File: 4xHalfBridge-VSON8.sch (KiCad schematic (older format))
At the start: 76 parts, among them U1 VSON8_Nexfet, U2 VSON8_Nexfet, U3 VSON8_Nexfet, U4 VSON8_Nexfet, U5 VSON8_Nexfet, U6 VSON8_Nexfet, U7 VSON8_Nexfet, U8 VSON8_Nexfet, U9 PowerStage_L

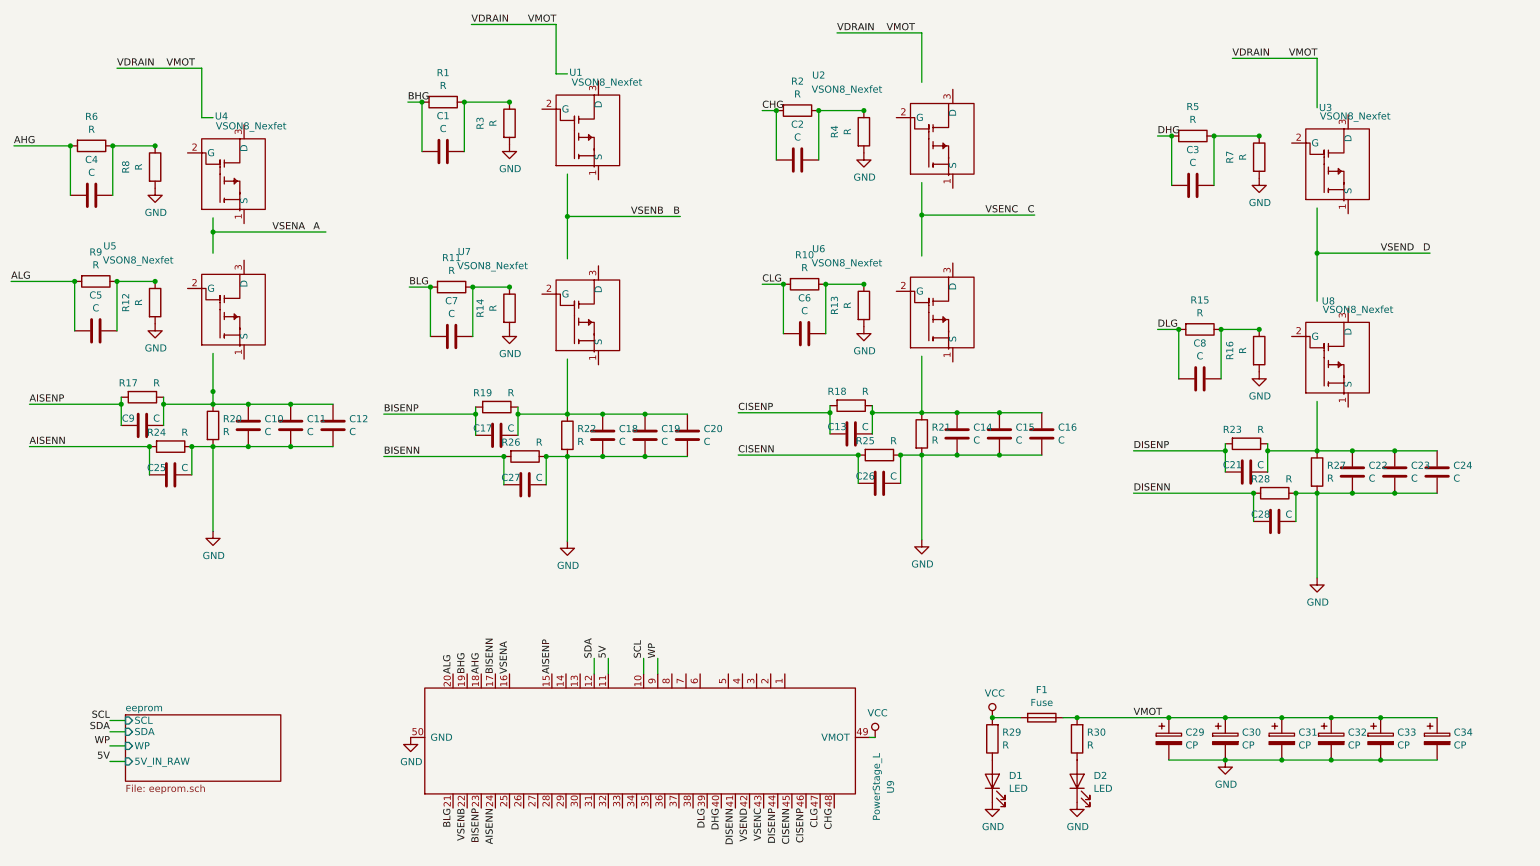
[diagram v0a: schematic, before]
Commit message: add voltage divider circuit for motor coil outpus
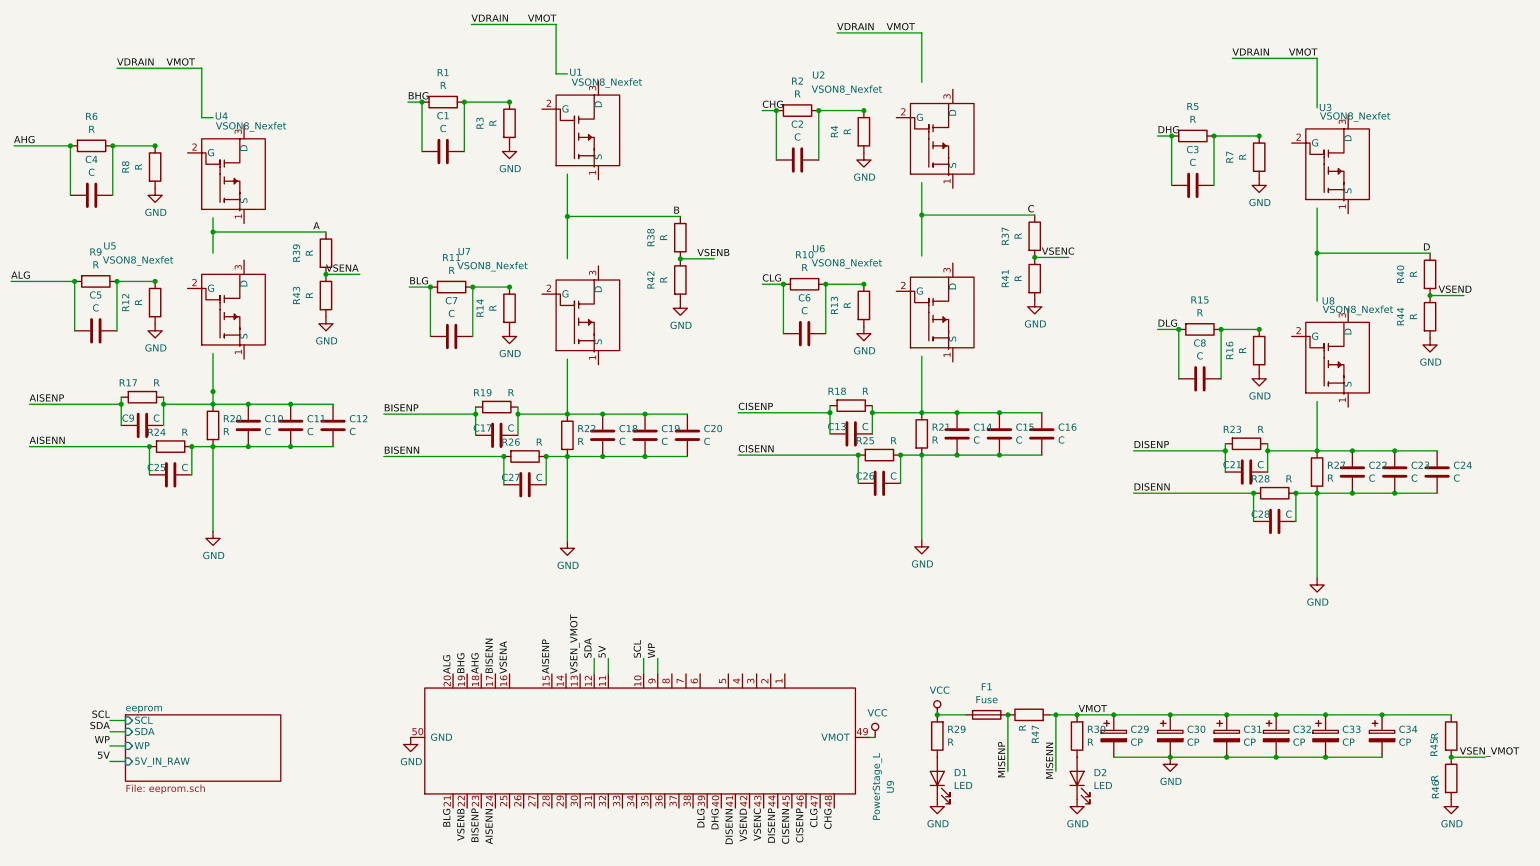
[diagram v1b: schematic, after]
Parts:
- added R37, R38, R39, R40, R41, R42, R43, R44, R45, R46: R, Resistor_SMD:R_0603_1608Metric_Pad1.05x0.95mm_HandSolder, symbol Device:R
- added R47: R, Resistor_SMD:R_1210_3225Metric_Pad1.42x2.65mm_HandSolder, symbol Device:R
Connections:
- net labels added: MISENN, MISENP, VSEN_VMOT
- wire segments 150 -> 159
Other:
- moved on the sheet: C29, C30, C31, C32, C33, C34, D1, D2, F1, R29, R30

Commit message: re route pcb-re arrange schematics
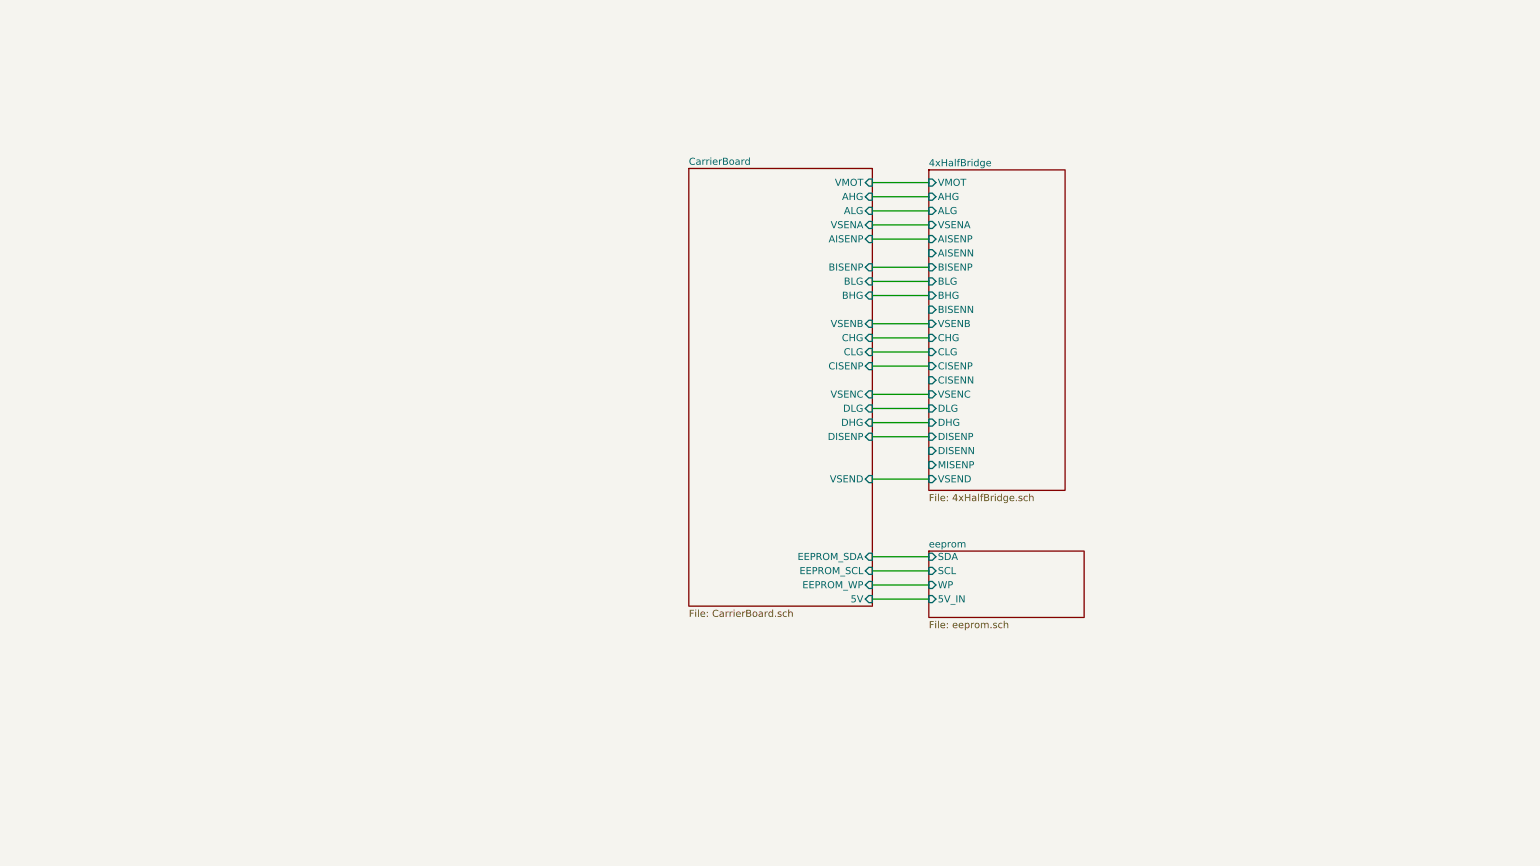
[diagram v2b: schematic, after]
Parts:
- removed C1, C10, C11, C12, C13, C14, C15, C16, C17, C18, C19, C2, C20, C21, C22, C23, C24, C25, C26, C27, C28, C3, C4, C5, C6, C7, C8, C9: C, Capacitor_SMD:C_0603_1608Metric_Pad1.05x0.95mm_HandSolder, symbol Device:C
- removed C29, C30: CP, Capacitor_THT:CP_Radial_D10.0mm_P5.00mm, symbol Device:CP
- removed C31, C32, C33, C34: CP, Capacitor_THT:CP_Radial_D5.0mm_P2.50mm, symbol Device:CP
- removed D1, D2: LED, LED_SMD:LED_0603_1608Metric_Pad1.05x0.95mm_HandSolder, symbol Device:LED
- removed F1: Fuse, Fuse:Fuse_1210_3225Metric_Pad1.42x2.65mm_HandSolder, symbol Device:Fuse
- removed R1, R10, R11, R12, R13, R14, R15, R16, R17, R18, R19, R2, R23, R24, R25, R26, R28, R29, R3, R30, R37, R38, R39, R4, R40, R41, R42, R43, R44, R45, R46, R5, R6, R7, R8, R9: R, Resistor_SMD:R_0603_1608Metric_Pad1.05x0.95mm_HandSolder, symbol Device:R
- removed R20, R21, R22, R27: R, Resistor_SMD:R_1806_4516Metric_Pad1.57x1.80mm_HandSolder, symbol Device:R
- removed R47: R, Resistor_SMD:R_1210_3225Metric_Pad1.42x2.65mm_HandSolder, symbol Device:R
- removed U1, U2, U3, U4, U5, U6, U7, U8: VSON8_Nexfet, Custom_Mosfet:MOSFET_CSD19531Q5A, symbol Custom_Fet:VSON8_Nexfet
- removed U9: PowerStage_L, sDrive_Carriers:PowerStage_Carrier_L, symbol sDrive_Carriers:PowerStage_L
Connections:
- net labels removed: 5V, A, AHG, AISENN, AISENP, ALG, B, BHG, BISENN, BISENP, BLG, C, CHG, CISENN, CISENP, CLG, D, DHG, DISENN, DISENP, DLG, GND, MISENN, MISENP, SCL, SDA, VCC, VDRAIN, VMOT, VSENA, VSENB, VSENC, VSEND, VSEN_VMOT, WP
- wire segments 159 -> 21
